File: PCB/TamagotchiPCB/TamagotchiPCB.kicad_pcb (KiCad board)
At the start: 2 copper layers, 58.8 x 99.5 mm, 9 parts, among them U1 ESP32_DevKit_V1_DOIT

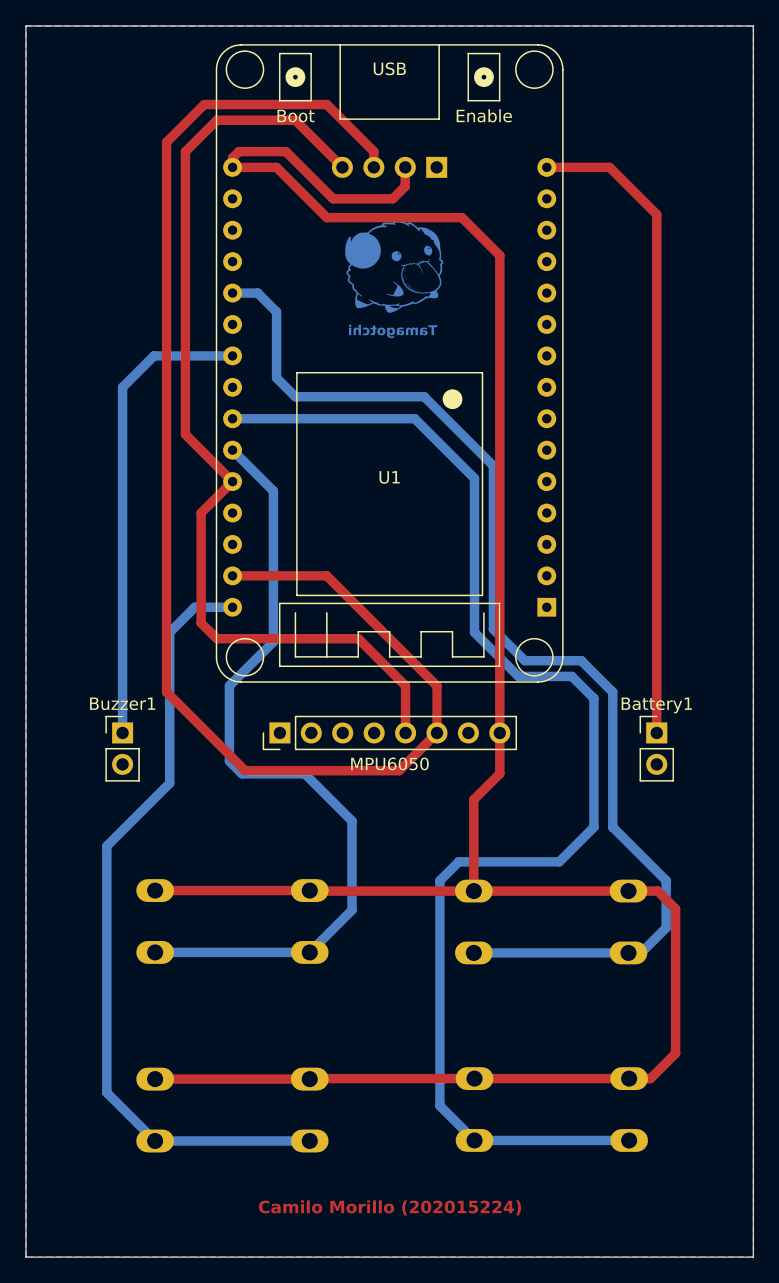
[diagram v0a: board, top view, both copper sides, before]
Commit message: edit pcb imagenes
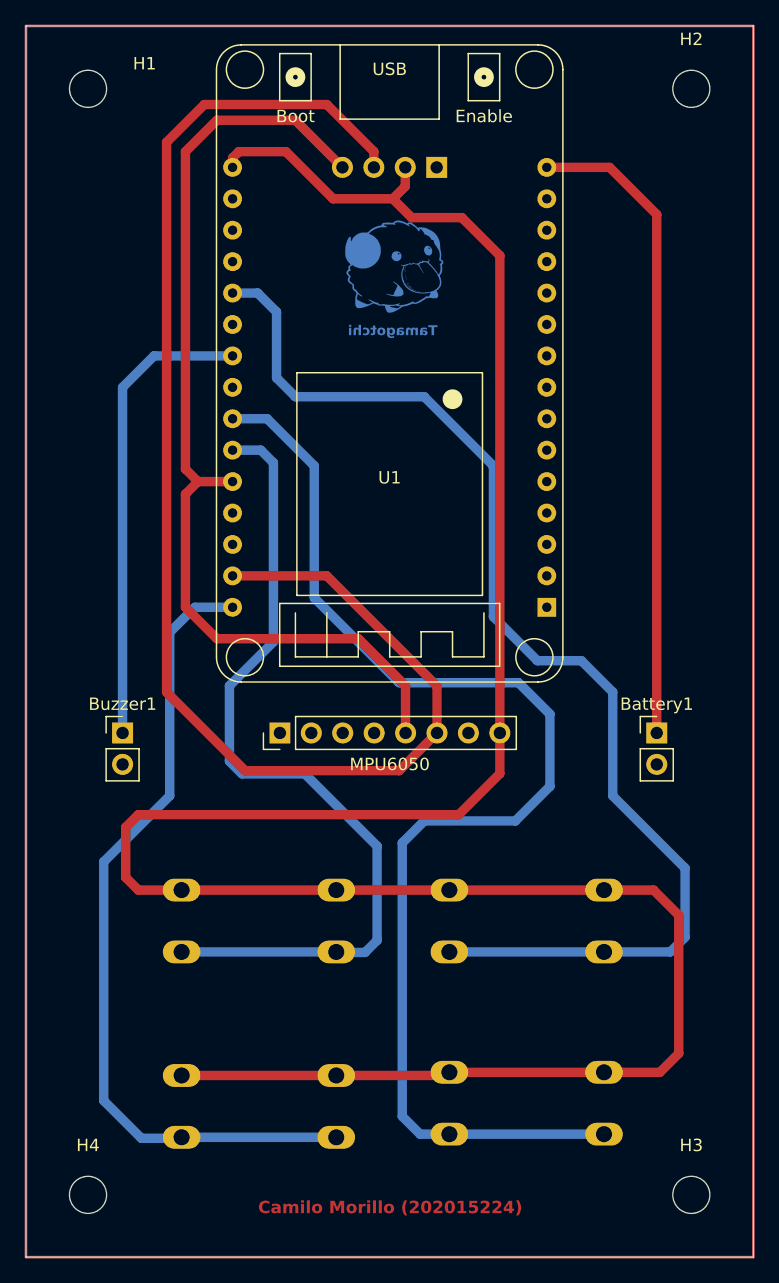
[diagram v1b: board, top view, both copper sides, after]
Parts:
- added H1: MountingHole, MountingHole:MountingHole_3mm, F.Cu at (143.3, 47.0)
- added H2: MountingHole, MountingHole:MountingHole_3mm, F.Cu at (192.0, 47.0)
- added H3: MountingHole, MountingHole:MountingHole_3mm, F.Cu at (192.0, 136.4)
- added H4: MountingHole, MountingHole:MountingHole_3mm, F.Cu at (143.3, 136.4)
- moved Enter1 2.16 mm to (163.3, 126.7)
- moved Right1 2.14 mm to (163.3, 111.8)
- moved Back1 2.09 mm to (185.0, 126.5)
- moved Left1 1.98 mm to (185.0, 111.8)
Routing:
- net 3.3V: track 192.6 -> 205.1 mm
- net Back: track 105.2 -> 100.5 mm
- net Left: track 92.2 -> 96.1 mm
- net Enter: track 63.2 -> 66.1 mm
- net Right: track 64.4 -> 66.9 mm
- net SDA: track 78.5 -> 80.0 mm
